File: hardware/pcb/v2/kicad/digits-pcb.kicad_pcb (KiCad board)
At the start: 2 copper layers, 76.2 x 56.9 mm, 71 parts, among them J1 Conn_02x20_Odd_Even, J3 VIN_BARREL_PIGTAIL, J4 Conn_01x07, J6 Conn_01x02, J7 Screw_Terminal_01x02, J8 Conn_01x04, J9 Conn_01x03, SW1 SW_Push, U1 LM2596S-5, U2 DRV8871DDAR, U3 RP2040, U4 W25Q16JVSSIQ, U5 AMS1117-3.3, U6 TLV320AIC3104IRHBR, U7 XC6206P182MR, Y1 ABM8-272-T3

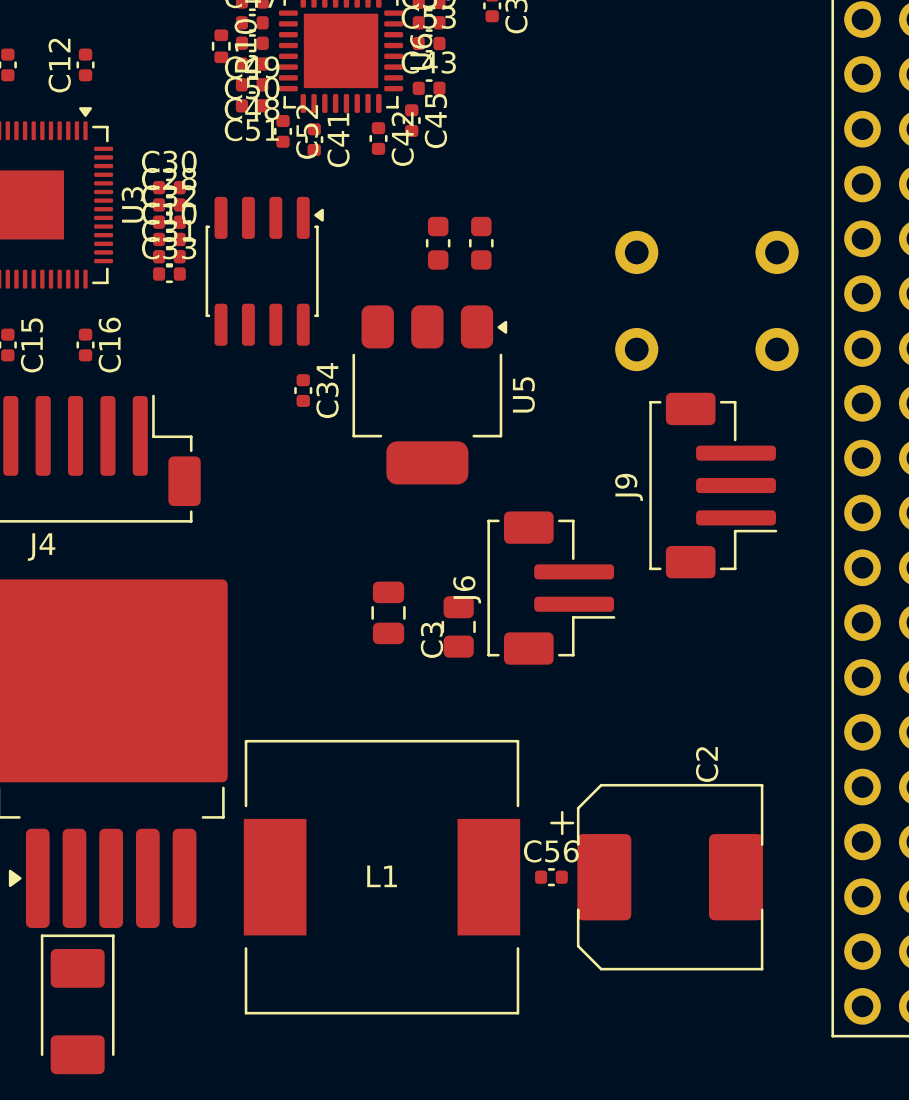
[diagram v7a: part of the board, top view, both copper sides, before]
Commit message: feat(hardware): zero real DRC violations milestone
All 7 cluster placement checkers pass (50/50 constraints), all subsheet
and symbol invariants green, and kicad-cli DRC reports zero shorts,
clearance violations, courtyard overlaps, or solder mask bridges.

Final placement fix: respaced the RP2040 +3V3/DVDD_1V1 decoupling column
(C10/C28/C30/C31/C32/C33) from 0.80 mm pitch to 1.00 mm pitch and shifted
the row 0.1 mm east, resolving both the 0.18 mm pad-to-pad Power class
clearance shortfall and the stacked 0402 courtyard overlaps. C2 nudged
east to clear C56 courtyard on the +5V output.

Remaining 194 items are cosmetic silk/thermal/unconnected/lib_mismatch
warnings that do not affect fabrication.
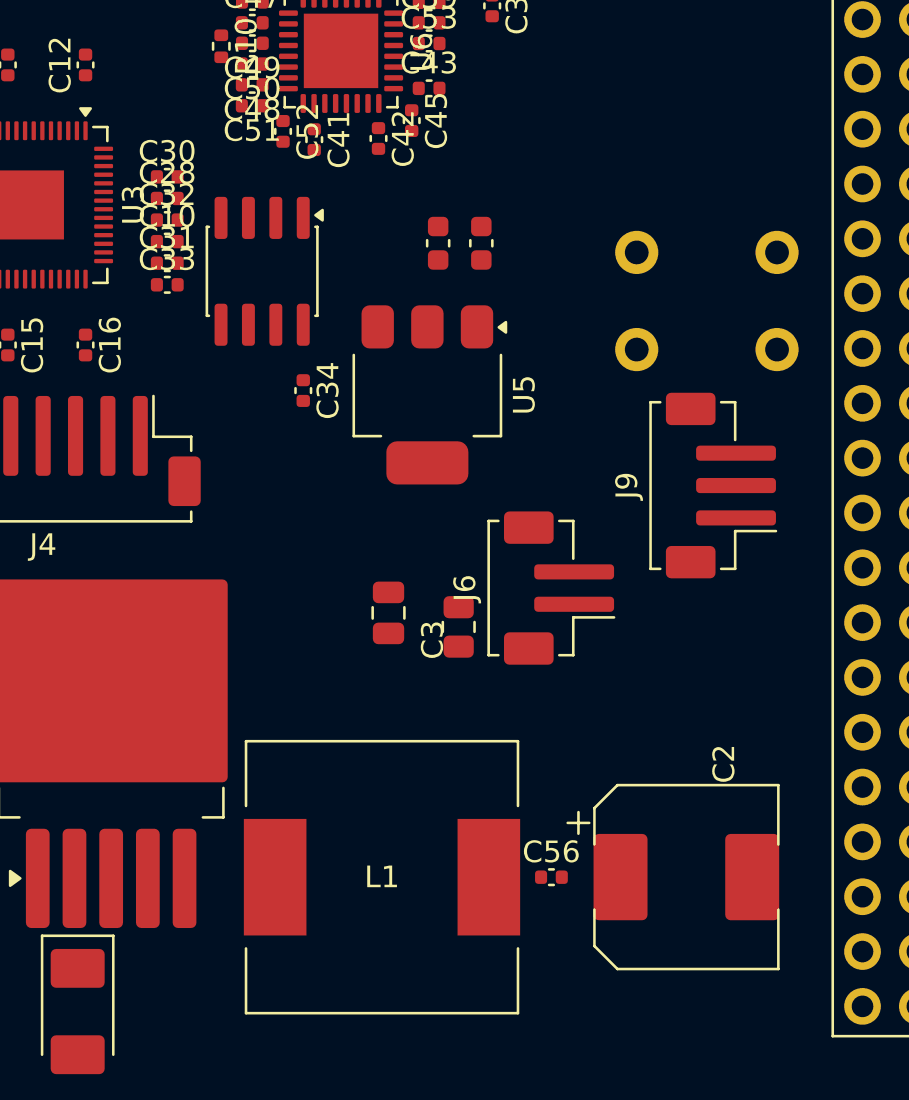
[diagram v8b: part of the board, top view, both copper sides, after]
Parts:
- moved C2 0.75 mm to (64.5, 60.6)
- moved C30 0.51 mm to (40.5, 28.2)
- moved C33 0.51 mm to (40.5, 33.2)
- moved C28 0.32 mm to (40.5, 29.2)
- moved C31 0.32 mm to (40.5, 32.2)
- moved C10 0.14 mm to (40.5, 31.2)
- moved C32 0.14 mm to (40.5, 30.2)
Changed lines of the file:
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@@
 	(footprint "Capacitor_SMD:C_0402_1005Metric"
 		(layer "F.Cu")
-		(at 40.6 30.31)
+		(at 40.5 30.21)
 		(descr "Capacitor SMD 0402 (1005 Metric), square (rectangular) end terminal, IPC-7351 nominal, (Body size source: IPC-SM-782 page 76, https://www.pcb-3d.com/wordpress/wp-content/uploads/ipc-sm-782a_amendment_1_and_2.pdf)")
 		(tags "capacitor")
@@
 	(footprint "Capacitor_SMD:C_0402_1005Metric"
 		(layer "F.Cu")
-		(at 40.6 31.91)
+		(at 40.5 32.21)
 		(descr "Capacitor SMD 0402 (1005 Metric), square (rectangular) end terminal, IPC-7351 nominal, (Body size source: IPC-SM-782 page 76, https://www.pcb-3d.com/wordpress/wp-content/uploads/ipc-sm-782a_amendment_1_and_2.pdf)")
 		(tags "capacitor")
@@
 	(footprint "Capacitor_SMD:C_0402_1005Metric"
 		(layer "F.Cu")
-		(at 40.6 29.51)
+		(at 40.5 29.21)
 		(descr "Capacitor SMD 0402 (1005 Metric), square (rectangular) end terminal, IPC-7351 nominal, (Body size source: IPC-SM-782 page 76, https://www.pcb-3d.com/wordpress/wp-content/uploads/ipc-sm-782a_amendment_1_and_2.pdf)")
 		(tags "capacitor")
@@
 	(footprint "Capacitor_SMD:CP_Elec_8x6.5"
 		(layer "F.Cu")
-		(at 63.797889 60.654853)
+		(at 64.55 60.65)
 		(descr "SMD capacitor, aluminum electrolytic, Rubycon, 8.0x6.5mm")
 		(tags "capacitor electrolytic")
@@
 	(footprint "Capacitor_SMD:C_0402_1005Metric"
 		(layer "F.Cu")
-		(at 40.6 31.11)
+		(at 40.5 31.21)
 		(descr "Capacitor SMD 0402 (1005 Metric), square (rectangular) end terminal, IPC-7351 nominal, (Body size source: IPC-SM-782 page 76, https://www.pcb-3d.com/wordpress/wp-content/uploads/ipc-sm-782a_amendment_1_and_2.pdf)")
 		(tags "capacitor")
@@
 	(footprint "Capacitor_SMD:C_0402_1005Metric"
 		(layer "F.Cu")
-		(at 40.6 28.71)
+		(at 40.5 28.21)
 		(descr "Capacitor SMD 0402 (1005 Metric), square (rectangular) end terminal, IPC-7351 nominal, (Body size source: IPC-SM-782 page 76, https://www.pcb-3d.com/wordpress/wp-content/uploads/ipc-sm-782a_amendment_1_and_2.pdf)")
 		(tags "capacitor")
@@
 	(footprint "Capacitor_SMD:C_0402_1005Metric"
 		(layer "F.Cu")
-		(at 40.6 32.71)
+		(at 40.5 33.21)
 		(descr "Capacitor SMD 0402 (1005 Metric), square (rectangular) end terminal, IPC-7351 nominal, (Body size source: IPC-SM-782 page 76, https://www.pcb-3d.com/wordpress/wp-content/uploads/ipc-sm-782a_amendment_1_and_2.pdf)")
 		(tags "capacitor")
